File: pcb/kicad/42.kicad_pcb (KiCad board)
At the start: 2 copper layers, 326.8 x 113.5 mm, 100 parts, among them J1 USB_C_Receptacle, J2 USB_C_Receptacle, J3 USB_C_Receptacle, K1 KEYSW, K10 KEYSW, K11 KEYSW, K12 KEYSW, K13 KEYSW, K14 KEYSW, K15 KEYSW, K16 KEYSW, K17 KEYSW, K18 KEYSW, K19 KEYSW, K2 KEYSW, K20 KEYSW, K21 KEYSW, K22 KEYSW, K23 KEYSW, K24 KEYSW, K25 KEYSW, K26 KEYSW, K27 KEYSW, K28 KEYSW, K29 KEYSW, K3 KEYSW, K30 KEYSW, K31 KEYSW, K32 KEYSW, K33 KEYSW, K34 KEYSW, K35 KEYSW, K36 KEYSW, K37 KEYSW, K38 KEYSW, K39 KEYSW, K4 KEYSW, K40 KEYSW, K41 KEYSW, K42 KEYSW, K5 KEYSW, K6 KEYSW, K7 KEYSW, K8 KEYSW, K9 KEYSW, U1 TEENSY2.0

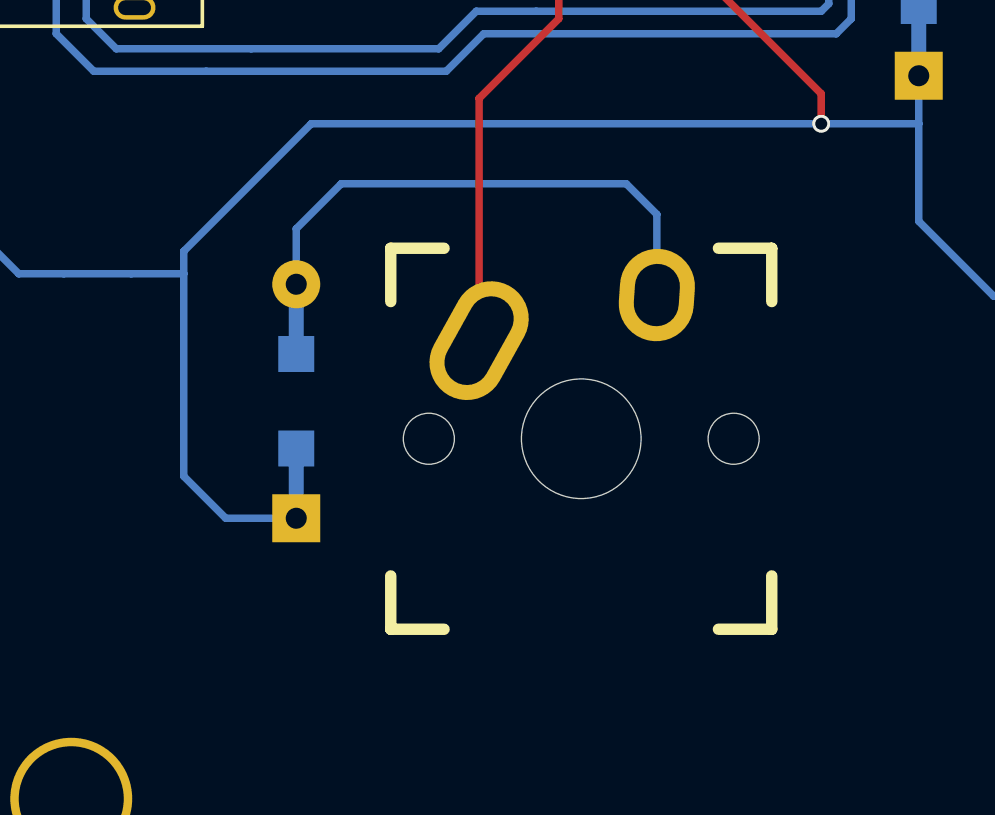
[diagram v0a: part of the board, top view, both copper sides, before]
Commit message: fixed position of thumb key footprint
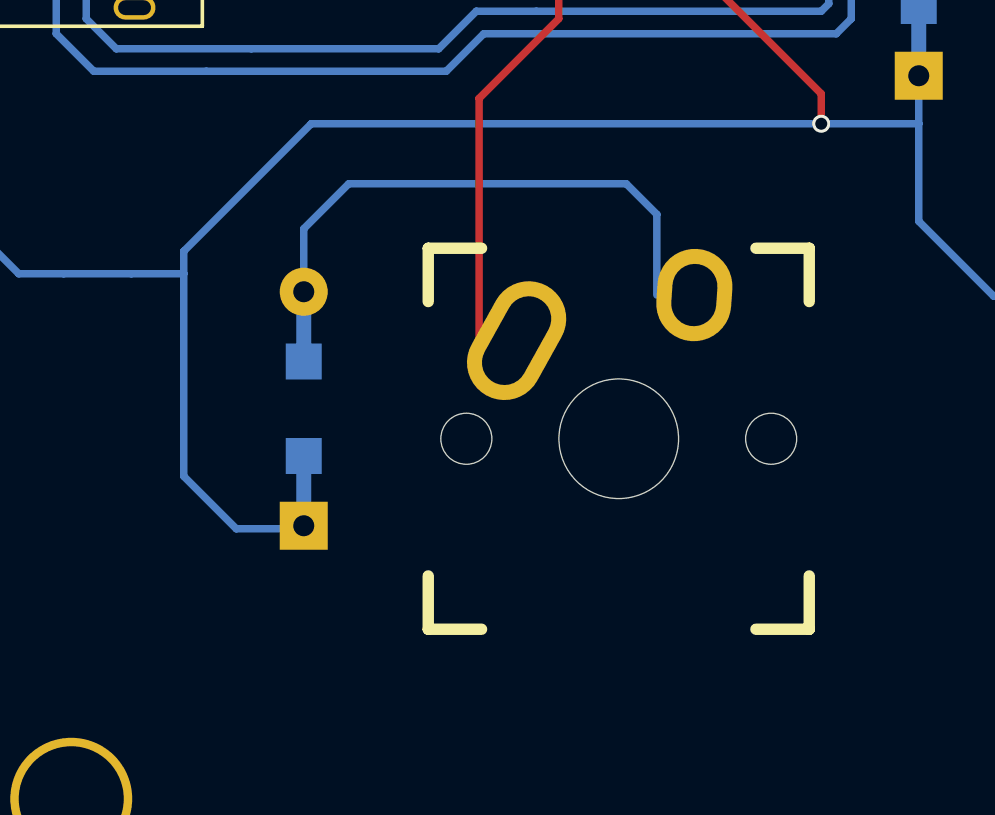
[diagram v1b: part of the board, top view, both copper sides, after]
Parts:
- moved K42 1.25 mm to (203.5, 108.5)
- moved D42 0.35 mm to (193.0, 107.5)
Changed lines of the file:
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@@
     (links 355)
     (no_connects 19)
-    (area 8.985 11.949999 173.865 213.300001)
+    (area 12.199999 11.949999 339.050001 125.550001)
     (thickness 1.6)
     (drawings 44)
@@
   )
   (module keyboard_parts:D_SOD123_axial (layer B.Cu)
-    (at 192.75 107.25 90)
+    (at 193 107.5 90)
     (attr smd)
     (fp_text reference D42 (at 0 -1.925 90) (layer B.SilkS)
@@
   )
   (module keebs:Mx_Alps_100 (layer F.Cu)
-    (at 202.25 108.5)
+    (at 203.5 108.5)
     (descr MXALPS)
     (tags MXALPS)
@@
   (segment (start 166.25 100) (end 166.25 93.25) (width 0.25) (layer B.Cu) (net 23))
   (segment (start 164.25 102) (end 166.25 100) (width 0.25) (layer B.Cu) (net 23))
-  (segment (start 192.75 111.15) (end 190.4 111.15) (width 0.25) (layer B.Cu) (net 23))
+  (segment (start 193 111.5) (end 190.75 111.5) (width 0.25) (layer B.Cu) (net 23) (status 10))
   (segment (start 193.25 98) (end 210.25 98) (width 0.25) (layer B.Cu) (net 23))
   (segment (start 210.25 98) (end 213.5 98) (width 0.25) (layer B.Cu) (net 23))
@@
   (segment (start 189 109.75) (end 189 103) (width 0.25) (layer B.Cu) (net 23))
   (segment (start 189 103) (end 189 102.25) (width 0.25) (layer B.Cu) (net 23))
-  (segment (start 190.4 111.15) (end 189 109.75) (width 0.25) (layer B.Cu) (net 23))
+  (segment (start 190.75 111.5) (end 189 109.75) (width 0.25) (layer B.Cu) (net 23))
   (segment (start 233.25 94.4) (end 233.25 100.5) (width 0.25) (layer B.Cu) (net 23))
   (segment (start 213.5 101.25) (end 213.5 98) (width 0.25) (layer B.Cu) (net 23))
@@
   (segment (start 245.27 83.77) (end 244.25 82.75) (width 0.25) (layer B.Cu) (net 88))
   (segment (start 204.77 103.71) (end 204.77 101.02) (width 0.25) (layer B.Cu) (net 89))
-  (segment (start 192.75 101.5) (end 192.75 103.35) (width 0.25) (layer B.Cu) (net 89))
-  (segment (start 194.25 100) (end 192.75 101.5) (width 0.25) (layer B.Cu) (net 89))
-  (segment (start 203.75 100) (end 194.25 100) (width 0.25) (layer B.Cu) (net 89))
+  (segment (start 193 101.5) (end 193 103.6) (width 0.25) (layer B.Cu) (net 89) (status 800020))
+  (segment (start 194.5 100) (end 193 101.5) (width 0.25) (layer B.Cu) (net 89))
+  (segment (start 203.75 100) (end 194.5 100) (width 0.25) (layer B.Cu) (net 89))
   (segment (start 204.77 101.02) (end 203.75 100) (width 0.25) (layer B.Cu) (net 89))
   (segment (start 147.7 24.96) (end 147.7 26.22) (width 0.25) (layer F.Cu) (net 97))

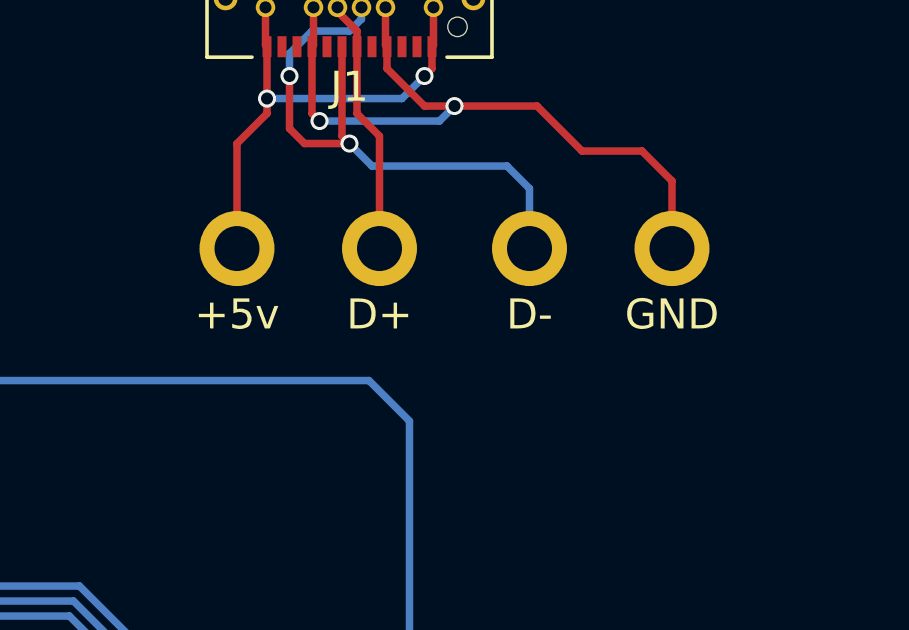
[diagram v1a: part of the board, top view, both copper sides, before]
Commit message: fixed inverted connections on USB receptacle
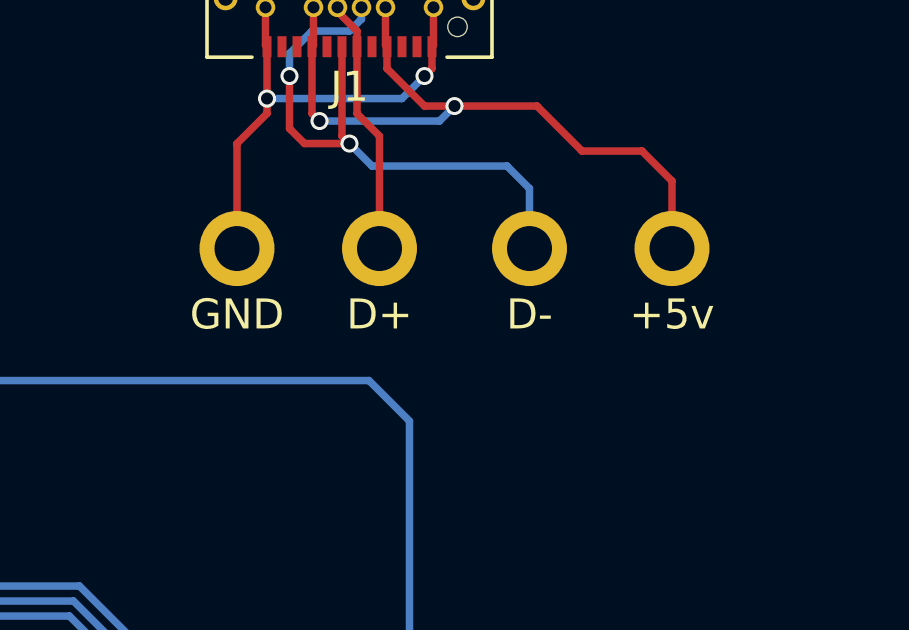
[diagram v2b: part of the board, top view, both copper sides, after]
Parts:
- PIN1: value +5v -> GND
- PIN4: value GND -> +5v
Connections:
- J1 pad A1: /+5v -> /GND
- J1 pad A12: /+5v -> /GND
- J1 pad A4: /GND -> /+5v
- J1 pad A9: /GND -> /+5v
- J1 pad B1: /+5v -> /GND
- J1 pad B12: /+5v -> /GND
- J1 pad B4: /GND -> /+5v
- J1 pad B9: /GND -> /+5v
- PIN1 pad 1: /+5v -> /GND
- PIN4 pad 1: /GND -> /+5v
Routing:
- net /GND: track 24.0 -> 23.5 mm
- net /+5v: track 16.4 -> 16.9 mm
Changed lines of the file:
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@@
   (general
     (links 355)
-    (no_connects 19)
+    (no_connects 21)
     (area 12.199999 11.949999 339.050001 125.550001)
     (thickness 1.6)
@@
     (mod_text_size 1 1)
     (mod_text_width 0.15)
-    (pad_size 1.5 1.5)
-    (pad_drill 0.6)
+    (pad_size 2.5 2.5)
+    (pad_drill 1.5)
     (pad_to_mask_clearance 0)
     (aux_axis_origin 0 0)
@@
       (net 26 "Net-(J1-PadS1)"))
     (pad A1 smd rect (at -2.75 -5.02 180) (size 0.3 0.7) (layers F.Cu F.Paste F.Mask)
-      (net 97 /+5v))
+      (net 98 /GND))
     (pad A2 smd rect (at -2.25 -5.02 180) (size 0.3 0.7) (layers F.Cu F.Paste F.Mask)
       (net 27 "Net-(J1-PadA2)"))
@@
       (net 28 "Net-(J1-PadA3)"))
     (pad A4 smd rect (at -1.25 -5.02 180) (size 0.3 0.7) (layers F.Cu F.Paste F.Mask)
-      (net 98 /GND))
+      (net 97 /+5v))
     (pad A5 smd rect (at -0.75 -5.02 180) (size 0.3 0.7) (layers F.Cu F.Paste F.Mask)
       (net 29 "Net-(J1-PadA5)"))
@@
       (net 100 /D-))
     (pad A12 smd rect (at 2.75 -5.02 180) (size 0.3 0.7) (layers F.Cu F.Paste F.Mask)
-      (net 97 /+5v))
+      (net 98 /GND))
     (pad A10 smd rect (at 1.75 -5.02 180) (size 0.3 0.7) (layers F.Cu F.Paste F.Mask)
       (net 30 "Net-(J1-PadA10)"))
     (pad A9 smd rect (at 1.25 -5.02 180) (size 0.3 0.7) (layers F.Cu F.Paste F.Mask)
-      (net 98 /GND))
+      (net 97 /+5v))
     (pad A8 smd rect (at 0.75 -5.02 180) (size 0.3 0.7) (layers F.Cu F.Paste F.Mask)
       (net 31 "Net-(J1-PadA8)"))
@@
     (pad "" np_thru_hole circle (at -3.6 -4.36 180) (size 0.65 0.65) (drill 0.65) (layers *.Cu *.Mask))
     (pad B1 thru_hole circle (at 2.8 -3.71 180) (size 0.65 0.65) (drill 0.4) (layers *.Cu *.Mask)
-      (net 97 /+5v))
-    (pad B4 thru_hole circle (at 1.2 -3.71 180) (size 0.65 0.65) (drill 0.4) (layers *.Cu *.Mask)
       (net 98 /GND))
+    (pad B4 thru_hole circle (at 1.2 -3.71 180) (size 0.65 0.65) (drill 0.4) (layers *.Cu *.Mask)
+      (net 97 /+5v))
     (pad B6 thru_hole circle (at 0.4 -3.71 180) (size 0.65 0.65) (drill 0.4) (layers *.Cu *.Mask)
       (net 99 /D+))
@@
       (net 100 /D-))
     (pad B9 thru_hole circle (at -1.2 -3.71 180) (size 0.65 0.65) (drill 0.4) (layers *.Cu *.Mask)
-      (net 98 /GND))
-    (pad B12 thru_hole circle (at -2.8 -3.71 180) (size 0.65 0.65) (drill 0.4) (layers *.Cu *.Mask)
       (net 97 /+5v))
+    (pad B12 thru_hole circle (at -2.8 -3.71 180) (size 0.65 0.65) (drill 0.4) (layers *.Cu *.Mask)
+      (net 98 /GND))
     (pad B2 thru_hole circle (at 2.4 -3.01 180) (size 0.65 0.65) (drill 0.4) (layers *.Cu *.Mask)
       (net 33 "Net-(J1-PadB2)"))
@@
       (effects (font (size 1 1) (thickness 0.15)))
     )
-    (fp_text value +5v (at 0 2.2) (layer F.SilkS)
+    (fp_text value GND (at 0 2.2) (layer F.SilkS)
       (effects (font (size 1 1) (thickness 0.15)))
     )
     (pad 1 thru_hole circle (at 0 0) (size 2.5 2.5) (drill 1.5) (layers *.Cu *.Mask F.SilkS)
-      (net 97 /+5v))
+      (net 98 /GND))
   )
   (module footprints:1pin-small (layer F.Cu)
@@
       (effects (font (size 1 1) (thickness 0.15)))
     )
-    (fp_text value GND (at 0 2.2) (layer F.SilkS)
+    (fp_text value +5v (at 0 2.2) (layer F.SilkS)
       (effects (font (size 1 1) (thickness 0.15)))
     )
     (pad 1 thru_hole circle (at 0 0) (size 2.5 2.5) (drill 1.5) (layers *.Cu *.Mask F.SilkS)
-      (net 98 /GND))
+      (net 97 /+5v))
   )
   (gr_line (start 260 98.25) (end 265 93.25) (angle 90) (layer Edge.Cuts) (width 0.1))
@@
   (segment (start 245.27 83.77) (end 244.25 82.75) (width 0.25) (layer B.Cu) (net 88))
   (segment (start 204.77 103.71) (end 204.77 101.02) (width 0.25) (layer B.Cu) (net 89))
-  (segment (start 193 101.5) (end 193 103.6) (width 0.25) (layer B.Cu) (net 89) (status 800020))
+  (segment (start 193 101.5) (end 193 103.6) (width 0.25) (layer B.Cu) (net 89) (status 20))
   (segment (start 194.5 100) (end 193 101.5) (width 0.25) (layer B.Cu) (net 89))
   (segment (start 203.75 100) (end 194.5 100) (width 0.25) (layer B.Cu) (net 89))
   (segment (start 204.77 101.02) (end 203.75 100) (width 0.25) (layer B.Cu) (net 89))
-  (segment (start 147.7 24.96) (end 147.7 26.22) (width 0.25) (layer F.Cu) (net 97))
-  (segment (start 147.7 26.22) (end 147.75 26.27) (width 0.25) (layer F.Cu) (net 97))
-  (segment (start 153.3 24.96) (end 153.3 26.22) (width 0.25) (layer F.Cu) (net 97))
-  (segment (start 153.3 26.22) (end 153.25 26.27) (width 0.25) (layer F.Cu) (net 97))
-  (segment (start 153.25 26.27) (end 153.25 27) (width 0.25) (layer F.Cu) (net 97))
-  (via (at 147.75 28) (size 0.6) (drill 0.4) (layers F.Cu B.Cu) (net 97))
-  (segment (start 152.25 28) (end 147.75 28) (width 0.25) (layer B.Cu) (net 97))
-  (segment (start 153 27.25) (end 152.25 28) (width 0.25) (layer B.Cu) (net 97))
-  (via (at 153 27.25) (size 0.6) (drill 0.4) (layers F.Cu B.Cu) (net 97))
-  (segment (start 153.25 27) (end 153 27.25) (width 0.25) (layer F.Cu) (net 97))
-  (segment (start 147.75 26.27) (end 147.75 28) (width 0.25) (layer F.Cu) (net 97))
-  (segment (start 147.75 28) (end 147.75 28.5) (width 0.25) (layer F.Cu) (net 97))
   (segment (start 146.75 29.5) (end 146.75 33) (width 0.25) (layer F.Cu) (net 97))
-  (segment (start 147.75 28.5) (end 146.75 29.5) (width 0.25) (layer F.Cu) (net 97))
-  (segment (start 149.3 24.96) (end 149.3 26.22) (width 0.25) (layer F.Cu) (net 98))
-  (segment (start 149.3 26.22) (end 149.25 26.27) (width 0.25) (layer F.Cu) (net 98))
-  (segment (start 151.7 24.96) (end 151.7 26.22) (width 0.25) (layer F.Cu) (net 98))
-  (segment (start 151.7 26.22) (end 151.75 26.27) (width 0.25) (layer F.Cu) (net 98))
-  (segment (start 149.25 26.27) (end 149.25 28.5) (width 0.25) (layer F.Cu) (net 98))
-  (via (at 154 28.25) (size 0.6) (drill 0.4) (layers F.Cu B.Cu) (net 98))
-  (segment (start 153.5 28.75) (end 154 28.25) (width 0.25) (layer B.Cu) (net 98))
-  (segment (start 149.5 28.75) (end 153.5 28.75) (width 0.25) (layer B.Cu) (net 98))
-  (via (at 149.5 28.75) (size 0.6) (drill 0.4) (layers F.Cu B.Cu) (net 98))
-  (segment (start 149.25 28.5) (end 149.5 28.75) (width 0.25) (layer F.Cu) (net 98))
-  (segment (start 151.75 26.27) (end 151.75 27) (width 0.25) (layer F.Cu) (net 98))
+  (segment (start 149.3 24.96) (end 149.3 26.22) (width 0.25) (layer F.Cu) (net 97))
+  (segment (start 149.3 26.22) (end 149.25 26.27) (width 0.25) (layer F.Cu) (net 97))
+  (segment (start 151.7 24.96) (end 151.7 26.22) (width 0.25) (layer F.Cu) (net 97))
+  (segment (start 151.7 26.22) (end 151.75 26.27) (width 0.25) (layer F.Cu) (net 97))
+  (segment (start 149.25 26.27) (end 149.25 28.5) (width 0.25) (layer F.Cu) (net 97))
+  (via (at 154 28.25) (size 0.6) (drill 0.4) (layers F.Cu B.Cu) (net 97))
+  (segment (start 153.5 28.75) (end 154 28.25) (width 0.25) (layer B.Cu) (net 97))
+  (segment (start 149.5 28.75) (end 153.5 28.75) (width 0.25) (layer B.Cu) (net 97))
+  (via (at 149.5 28.75) (size 0.6) (drill 0.4) (layers F.Cu B.Cu) (net 97))
+  (segment (start 149.25 28.5) (end 149.5 28.75) (width 0.25) (layer F.Cu) (net 97))
+  (segment (start 151.75 26.27) (end 151.75 27) (width 0.25) (layer F.Cu) (net 97))
+  (segment (start 153 28.25) (end 154 28.25) (width 0.25) (layer F.Cu) (net 97))
+  (segment (start 151.75 27) (end 153 28.25) (width 0.25) (layer F.Cu) (net 97))
+  (segment (start 147.7 24.96) (end 147.7 26.22) (width 0.25) (layer F.Cu) (net 98))
+  (segment (start 147.7 26.22) (end 147.75 26.27) (width 0.25) (layer F.Cu) (net 98))
+  (segment (start 153.3 24.96) (end 153.3 26.22) (width 0.25) (layer F.Cu) (net 98))
+  (segment (start 153.3 26.22) (end 153.25 26.27) (width 0.25) (layer F.Cu) (net 98))
+  (segment (start 153.25 26.27) (end 153.25 27) (width 0.25) (layer F.Cu) (net 98))
+  (via (at 147.75 28) (size 0.6) (drill 0.4) (layers F.Cu B.Cu) (net 98))
+  (segment (start 152.25 28) (end 147.75 28) (width 0.25) (layer B.Cu) (net 98))
+  (segment (start 153 27.25) (end 152.25 28) (width 0.25) (layer B.Cu) (net 98))
+  (via (at 153 27.25) (size 0.6) (drill 0.4) (layers F.Cu B.Cu) (net 98))
+  (segment (start 153.25 27) (end 153 27.25) (width 0.25) (layer F.Cu) (net 98))
+  (segment (start 147.75 26.27) (end 147.75 28) (width 0.25) (layer F.Cu) (net 98))
+  (segment (start 147.75 28) (end 147.75 28.5) (width 0.25) (layer F.Cu) (net 98))
+  (segment (start 147.75 28.5) (end 146.75 29.5) (width 0.25) (layer F.Cu) (net 98))
   (segment (start 161.25 30.75) (end 161.25 33) (width 0.25) (layer F.Cu) (net 98))
   (segment (start 160.25 29.75) (end 161.25 30.75) (width 0.25) (layer F.Cu) (net 98))
   (segment (start 158.25 29.75) (end 160.25 29.75) (width 0.25) (layer F.Cu) (net 98))
   (segment (start 156.75 28.25) (end 158.25 29.75) (width 0.25) (layer F.Cu) (net 98))
-  (segment (start 153 28.25) (end 154 28.25) (width 0.25) (layer F.Cu) (net 98))
   (segment (start 154 28.25) (end 156.75 28.25) (width 0.25) (layer F.Cu) (net 98))
-  (segment (start 151.75 27) (end 153 28.25) (width 0.25) (layer F.Cu) (net 98))
   (segment (start 150.1 24.96) (end 150.1 25.1) (width 0.25) (layer F.Cu) (net 99))
   (segment (start 150.1 25.1) (end 150.75 25.75) (width 0.25) (layer F.Cu) (net 99))
